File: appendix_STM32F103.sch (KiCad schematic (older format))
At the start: 0 parts

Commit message: added FTDI chip
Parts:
- added U?: STM32F103ZETx, Package_QFP:LQFP-144_20x20mm_P0.5mm, symbol MCU_ST_STM32F1:STM32F103ZETx
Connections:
- new net +3V3: U?.108 (VDD), U?.121 (VDD), U?.131 (VDD), U?.144 (VDD), U?.17 (VDD), U?.33 (VDDA), U?.39 (VDD), U?.52 (VDD), U?.6 (VBAT), U?.62 (VDD), U?.72 (VDD), U?.84 (VDD), U?.95 (VDD)
- new net GND: U?.107 (VSS), U?.120 (VSS), U?.130 (VSS), U?.143 (VSS), U?.16 (VSS), U?.30 (VSSA), U?.38 (VSS), U?.51 (VSS), U?.61 (VSS), U?.71 (VSS), U?.83 (VSS), U?.94 (VSS)

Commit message: merged hierarchical schematics
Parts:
- added C? (x7): 100n, symbol Device:C
- added C? (x2): 20p, symbol Device:C
- added C?: 10u, symbol Device:CP
- added FB?: Ferrite_Bead, symbol Device:Ferrite_Bead_Small
- added J?: Conn_ARM_JTAG_SWD_20, symbol Connector:Conn_ARM_JTAG_SWD_20
- added R? (x6): 10k, symbol Device:R
- added SW?: SW_Push, symbol Switch:SW_Push
- added Y?: CRYSTAL-8MHZSMD-5X3.2, CRYSTAL-SMD-5X3.2-4PAD, symbol SparkFun-Clocks:CRYSTAL-8MHZSMD-5X3.2
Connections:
- net labels added: +3.3VA, JTAG_RESET, JTAG_TCK_SWCLK, JTAG_TDI, JTAG_TDO_SWO, JTAG_TMS_SWDIO, JTAG_TRST, STM_BOOT1
- wire segments 50 -> 129
- no-connect marks 0 -> 3
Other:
- moved on the sheet: U?

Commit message: pre Annotation 1
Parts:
- removed Y?: CRYSTAL-8MHZSMD-5X3.2, CRYSTAL-SMD-5X3.2-4PAD, symbol SparkFun-Clocks:CRYSTAL-8MHZSMD-5X3.2
- added C?: 100n, symbol Device:C
- added J?: Micro_SD_Card_Det, symbol Connector:Micro_SD_Card_Det
- added J? (x2): Conn_02x05_Counter_Clockwise, symbol Connector_Generic:Conn_02x05_Counter_Clockwise
- added Y?: Crystal_8MHZ, symbol Device:Crystal
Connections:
- net labels added: ADC_Temp_Bed, ADC_Temp_HotEnd, DP_Bed, DP_Fan_1, DP_Hotend_1, D_SPI_MISO, D_SPI_MOSI, D_SPI_SCK, D_TMC_CS_X, D_TMC_CS_Y, D_TMC_CS_Z1, D_TMC_DIR_X, D_TMC_DIR_Y, D_TMC_DIR_Z1, D_TMC_EN_X, D_TMC_EN_Y, D_TMC_EN_Z1, D_TMC_STEP_X, D_TMC_STEP_Y, D_TMC_STEP_Z1, MISO, MOSI, SCK, SDSS, SW_End_Filament, SW_End_X_min, SW_End_Y_min, SW_End_Z_min
- wire segments 129 -> 143
- no-connect marks 3 -> 4
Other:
- note added: "JTAG Connector"
- note added: "LCD / Display"
- note added: "SD Card"
- moved on the sheet: C?, FB?, R?, SW?, U?

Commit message: 1st annotation, footprints, netlist
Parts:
- C201, C202, C203, C204, C205, C206, C207, C208, C209, C210, C211: renamed from C?; footprint (none) -> Capacitors_SMD:C_0805
- FB201: renamed from FB?; footprint (none) -> Resistors_SMD:R_0805_HandSoldering
- J201: renamed from J?; footprint (none) -> Connector_Card:microSD_HC_Hirose_DM3D-SF
- J202, J203: renamed from J?; footprint (none) -> Connector_Multicomp:Multicomp_MC9A12-1034_2x05_P2.54mm_Vertical
- J204: renamed from J?; footprint (none) -> Connectors_Multicomp:Multicomp_MC9A12-2034_2x10x2.54mm_Straight
- R201, R202, R203, R204, R205, R206: renamed from R?; footprint (none) -> Resistors_SMD:R_0805
- SW201: renamed from SW?; footprint (none) -> Switches:TACTILE_SWITCH_SMD_5.2MM
- U201: renamed from U?; footprint Package_QFP:LQFP-144_20x20mm_P0.5mm -> Housings_QFP:LQFP-144_20x20mm_Pitch0.5mm
- Y201: renamed from Y?; footprint (none) -> Crystals:Crystal_SMD_HC49-SD
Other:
- note added: "sd detect ?"

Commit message: started layouting TMC2660
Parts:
- removed J204: Conn_ARM_JTAG_SWD_20, Connectors_Multicomp:Multicomp_MC9A12-2034_2x10x2.54mm_Straight, symbol Connector:Conn_ARM_JTAG_SWD_20
- removed R202: 10k, Resistors_SMD:R_0805, symbol Device:R
- added J204: Conn_ARM_JTAG_SWD_10, symbol Connector:Conn_ARM_JTAG_SWD_10
- added J205: Conn_02x03_ISP, Connector_PinHeader_2.54mm:PinHeader_2x03_P2.54mm_Vertical, symbol Connector_Generic:Conn_02x03_Odd_Even
- C201, C202, C203, C204, C205, C206, C207, C208, C209, C210, C211: footprint Capacitors_SMD:C_0805 -> Capacitors_SMD:C_0603
- R201, R203, R204, R205, R206: footprint Resistors_SMD:R_0805 -> Resistors_SMD:R_0603
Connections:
- wire segments 143 -> 142
- no-connect marks 4 -> 1

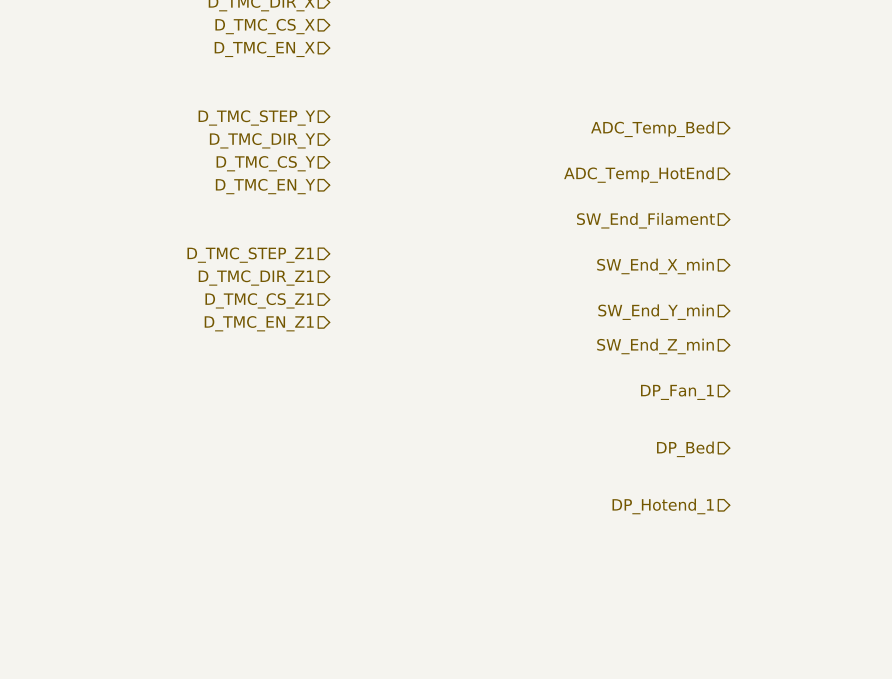
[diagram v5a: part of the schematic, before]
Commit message: Layout: all TMC / Schematic: Oli's comments
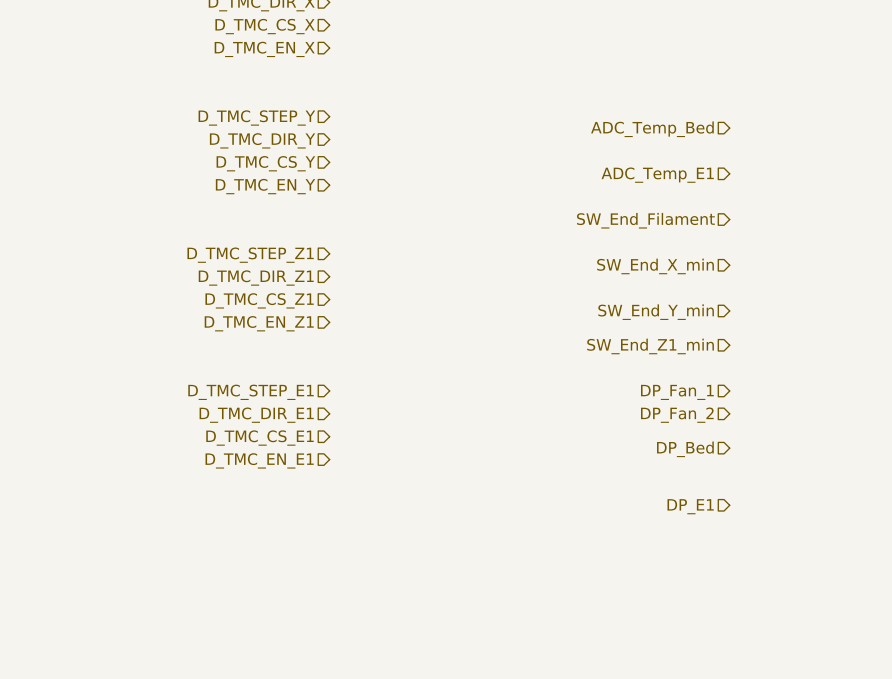
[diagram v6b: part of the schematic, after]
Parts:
- SW201: footprint Switches:TACTILE_SWITCH_SMD_5.2MM -> Button_Switch_SMD:SW_Push_1P1T_NO_CK_KMR2
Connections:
- net labels added: ADC_Temp_E1, DP_E1, DP_Fan_2, D_TMC_CS_E1, D_TMC_DIR_E1, D_TMC_EN_E1, D_TMC_STEP_E1, SW_End_Z1_min
- net labels removed: ADC_Temp_HotEnd, DP_Hotend_1, SW_End_Z_min
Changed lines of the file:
@@
 F 0 "SW201" V 6300 2350 50  0000 C CNN
 F 1 "SW_Push" V 5950 2400 50  0000 C CNN
-F 2 "Switches:TACTILE_SWITCH_SMD_5.2MM" H 6150 2350 50  0001 C CNN
+F 2 "Button_Switch_SMD:SW_Push_1P1T_NO_CK_KMR2" H 6150 2350 50  0001 C CNN
 F 3 "~" H 6150 2350 50  0001 C CNN
 	1    6150 2150
@@
 SW_End_Filament
 Text HLabel 3850 4500 0    50   Input ~ 0
-ADC_Temp_HotEnd
+ADC_Temp_E1
 Text HLabel 3850 4300 0    50   Input ~ 0
 ADC_Temp_Bed
@@
 SW_End_Y_min
 Text HLabel 3850 5250 0    50   Input ~ 0
-SW_End_Z_min
+SW_End_Z1_min
 Text HLabel 3850 5450 0    50   Input ~ 0
 DP_Fan_1
@@
 DP_Bed
 Text HLabel 3850 5950 0    50   Input ~ 0
-DP_Hotend_1
+DP_E1
 $Comp
 L Device:Crystal Y201
@@
 Wire Wire Line
 	14950 3250 15250 3250
+Text HLabel 3850 5550 0    50   Input ~ 0
+DP_Fan_2
+Text HLabel 2100 5750 0    50   Input ~ 0
+D_TMC_EN_E1
+Text HLabel 2100 5650 0    50   Input ~ 0
+D_TMC_CS_E1
+Text HLabel 2100 5450 0    50   Input ~ 0
+D_TMC_STEP_E1
+Text HLabel 2100 5550 0    50   Input ~ 0
+D_TMC_DIR_E1
 $EndSCHEMATC

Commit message: added footprints, layouted 3v3 Reg
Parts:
- SW201: footprint Button_Switch_SMD:SW_Push_1P1T_NO_CK_KMR2 -> Button_Switch_SMD:SW_SPST_KMR2
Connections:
- net labels added: ADC_Temp_MOSFET, D_INT_TMC_STALL_E1, D_INT_TMC_STALL_X, D_INT_TMC_STALL_Y, D_INT_TMC_STALL_Z1
- no-connect marks 1 -> 2

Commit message: corrected P.S. Schematic review
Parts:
- removed C203: 20p, Capacitors_SMD:C_0603, symbol Device:C
- removed C210: 10u, Capacitors_SMD:C_0603, symbol Device:CP
- removed C211: 100n, Capacitors_SMD:C_0603, symbol Device:C
- removed FB201: Ferrite_Bead, Resistors_SMD:R_0805_HandSoldering, symbol Device:Ferrite_Bead_Small
- removed J202, J203: Conn_02x05_Counter_Clockwise, Connector_Multicomp:Multicomp_MC9A12-1034_2x05_P2.54mm_Vertical, symbol Connector_Generic:Conn_02x05_Counter_Clockwise
- removed J205: Conn_02x03_ISP, Connector_PinHeader_2.54mm:PinHeader_2x03_P2.54mm_Vertical, symbol Connector_Generic:Conn_02x03_Odd_Even
- removed Y201: Crystal_8MHZ, Crystals:Crystal_SMD_HC49-SD, symbol Device:Crystal
- added J202: Conn_02x05_Odd_Even, symbol Connector_Generic:Conn_02x05_Odd_Even
- added R202, R207, R208: 100k, Resistors_SMD:R_0603, symbol Device:R
- added R209, R210, R211, R212: 200R, Resistors_SMD:R_0603, symbol Device:R
- added U202: NTS0104PW-Q100J, symbol FHNW-Pro4E-FS19T8-Library:NTS0104PW-Q100J
- added X201: SG-210STF, Oscillator:Oscillator_SMD_SeikoEpson_SG210-4Pin_2.5x2.0mm, symbol Oscillator:SG-210STF
- C202: value 20p -> 10n
- J201: footprint Connector_Card:microSD_HC_Hirose_DM3D-SF -> Connector_Card:microSD_HC_Hirose_DM3AT-SF-PEJM5
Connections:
- net labels added: 5V, Conn_LCD_CS, Conn_LCD_MOSI, Conn_LCD_SCK, D_LCD_Beeper, D_LCD_CS, D_LCD_Encoder_A, D_LCD_Encoder_B, D_LCD_Encoder_BTN, D_LCD_MOSI, D_LCD_Reset, D_LCD_SCK, RCC_OSC_IN
- net labels removed: ADC_Temp_Bed, ADC_Temp_E1, ADC_Temp_MOSFET, DP_Bed, DP_E1, DP_Fan_1, DP_Fan_2, D_SPI_MISO, D_SPI_MOSI, D_SPI_SCK, MISO, MOSI, SCK, SDSS, SW_End_Filament, SW_End_X_min, SW_End_Y_min, SW_End_Z1_min
- wire segments 142 -> 151
- no-connect marks 2 -> 3
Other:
- note added: "EXP3 Connector"
- note added: "Layout Datasheet p.1\nhttps://support.epson.biz/td/api/doc_check.php?dl=brief_SG-210STF&lang=en\n"
- note added: "OSC"
- note added: "pull-down on level shift lines ?"
- note added: "pull-up for #EN"
- moved on the sheet: J204, R203, R204, R205, R206
